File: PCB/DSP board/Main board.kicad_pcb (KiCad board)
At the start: 4 copper layers, 60 x 100 mm, 201 parts, among them J201 01x06 male SMD, J701 Conn_01x40_Female, J702 Conn_01x06_Female, J801 1140084168, J901 USB_B, U201 STM32H743II, U401 AS4C32M8SA, U501 CS42448, U601 MIC23050, U602 TPS2113A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

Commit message: Schematic updates + PCB placement
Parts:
- U604: footprint Housings_SSOP:TSOP-5_1.65x3.05mm_Pitch0.95mm -> TSOP-5:TSOP-5_1.65x3.05mm_Pitch0.95mm
- moved D101 252.8 mm to (254.5, 82.2)
- moved C614 238.9 mm to (253.6, 99.8), turned to 180 degrees
- moved C615 232.5 mm to (253.6, 101.0), turned to 180 degrees
- moved C504 231.7 mm to (248.2, 111.1), turned to 90 degrees
- moved C505 226.2 mm to (250.4, 115.3), turned to 270 degrees
- moved RN701 225.1 mm to (250.4, 32.6), turned to 270 degrees
- moved U604 224.8 mm to (253.5, 103.4), turned to 270 degrees
- moved C617 223.3 mm to (253.6, 105.8), turned to 180 degrees
- moved J801 222.1 mm to (226.4, 34.1)
- moved C503 219.0 mm to (231.6, 113.2), turned to 270 degrees
- moved RN702 215.0 mm to (251.7, 41.5), turned to 90 degrees
- moved RN703 213.4 mm to (246.6, 32.6), turned to 270 degrees
- moved C507 211.8 mm to (248.2, 113.9), turned to 270 degrees
- moved C506 209.2 mm to (240.9, 119.9), turned to 180 degrees
- moved RN705 202.0 mm to (242.4, 32.6), turned to 270 degrees
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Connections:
- RN502 pad 1: SAI2_SD_B -> Net-(RN502-Pad1)
- RN502 pad 2: SAI2_SCK_B -> SAI2_SD_B
- RN502 pad 3: SAI2_FS_B -> SAI2_SCK_B
- RN502 pad 4: Net-(RN502-Pad4) -> SAI2_FS_B
- RN502 pad 5: Net-(RN502-Pad5) -> DAC_LRCK
- RN502 pad 6: DAC_LRCK -> DAC_SCLK
- RN502 pad 7: DAC_SCLK -> DAC_SDIN1
- RN502 pad 8: DAC_SDIN1 -> Net-(RN502-Pad8)
- RN702 pad 1: Net-(RN702-Pad1) -> LCD_VSYNC
- RN702 pad 4: LCD_VSYNC -> Net-(RN702-Pad4)
- RN702 pad 5: TFT_VSD -> Net-(RN702-Pad5)
- RN702 pad 8: Net-(RN702-Pad8) -> TFT_VSD
- RN704 pad 1: LCD_B6 -> LCD_B0
- RN704 pad 2: LCD_B4 -> LCD_B2
- RN704 pad 3: LCD_B2 -> LCD_B4
- RN704 pad 4: LCD_B0 -> LCD_B6
- RN704 pad 5: TFT_B0 -> TFT_B6
- RN704 pad 6: TFT_B2 -> TFT_B4
- RN704 pad 7: TFT_B4 -> TFT_B2
- RN704 pad 8: TFT_B6 -> TFT_B0
- RN706 pad 1: LCD_G6 -> LCD_G0
- RN706 pad 2: LCD_G4 -> LCD_G2
- RN706 pad 3: LCD_G2 -> LCD_G4
- RN706 pad 4: LCD_G0 -> LCD_G6
- RN706 pad 5: TFT_G0 -> TFT_G6
- RN706 pad 6: TFT_G2 -> TFT_G4
- RN706 pad 7: TFT_G4 -> TFT_G2
- RN706 pad 8: TFT_G6 -> TFT_G0
- RN708 pad 1: LCD_R6 -> LCD_R0
- RN708 pad 2: LCD_R4 -> LCD_R2
- RN708 pad 3: LCD_R2 -> LCD_R4
- RN708 pad 4: LCD_R0 -> LCD_R6
- RN708 pad 5: TFT_R0 -> TFT_R6
- RN708 pad 6: TFT_R2 -> TFT_R4
- RN708 pad 7: TFT_R4 -> TFT_R2
- RN708 pad 8: TFT_R6 -> TFT_R0
- RN709 pad 1: TOUCH_NRESET -> TOUCH_NINT
- RN709 pad 2: TOUCH_NINT -> I2C1_SCL
- RN709 pad 3: I2C1_SCL -> I2C1_SDA
- RN709 pad 4: I2C1_SDA -> TOUCH_NRESET
- RN709 pad 5: TFT_SCL -> TFT_NRESET
- RN709 pad 7: TFT_NINT -> TFT_SCL
- RN709 pad 8: TFT_NRESET -> TFT_NINT
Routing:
- net GND: track 0.00 -> 855.7 mm, vias 0 -> 281
- added copper zone on B.Cu, net GND
- added copper zone on F.Cu, net GND

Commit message: Component Placement - RN
All components placed except for RAM Resistor Networks
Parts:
- removed C325: 1uF, Capacitors_SMD:C_0603
- removed C328: 10nF, Capacitors_SMD:C_0603
- moved R201 259.9 mm to (250.1, 66.8), turned to 90 degrees
- moved RN101 257.3 mm to (251.1, 83.7)
- moved RN102 251.8 mm to (253.2, 87.1), turned to 270 degrees
- moved R202 251.7 mm to (252.3, 79.5), turned to 270 degrees
- moved U603 243.1 mm to (238.6, 55.0), turned to 180 degrees
- moved D601 239.5 mm to (238.0, 52.9), turned to 180 degrees
- moved R606 235.1 mm to (235.1, 29.1), turned to 180 degrees
- moved C201 233.9 mm to (237.2, 61.5), turned to 270 degrees
- moved C701 233.3 mm to (236.2, 31.3)
- moved D602 231.4 mm to (234.6, 42.7), turned to 90 degrees
- moved C202 229.7 mm to (238.3, 61.5), turned to 270 degrees
- moved C702 228.5 mm to (236.5, 32.8)
- moved C205 227.4 mm to (251.3, 66.6), turned to 90 degrees
- moved C703 223.7 mm to (236.3, 34.2)
- moved L302 222.4 mm to (221.6, 59.7)
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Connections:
- D705 pad 1: TFT_NRESET -> TFT_SDA
- D705 pad 2: TFT_NINT -> TFT_NRESET
- D705 pad 4: TFT_SDA -> TFT_NINT
- D705 pad 7: TFT_SDA -> TFT_NINT
- D705 pad 8: TFT_NINT -> TFT_NRESET
- D705 pad 9: TFT_NRESET -> TFT_SDA
- RN709 pad 1: TOUCH_NINT -> I2C1_SDA
- RN709 pad 2: I2C1_SCL -> TOUCH_NRESET
- RN709 pad 3: I2C1_SDA -> TOUCH_NINT
- RN709 pad 4: TOUCH_NRESET -> I2C1_SCL
- RN709 pad 5: TFT_NRESET -> TFT_SCL
- RN709 pad 6: TFT_SDA -> TFT_NINT
- RN709 pad 7: TFT_SCL -> TFT_NRESET
- RN709 pad 8: TFT_NINT -> TFT_SDA
- RN801 pad 1: SDMMC1_D2 -> SDMMC1_CMD
- RN801 pad 4: SDMMC1_CMD -> SDMMC1_D2
- RN801 pad 5: SD_CMD -> SD_DAT2
- RN801 pad 8: SD_DAT2 -> SD_CMD
- RN802 pad 1: SDMMC1_CK -> SDMMC1_DETECT
- RN802 pad 2: SDMMC1_D0 -> SDMMC1_D1
- RN802 pad 3: SDMMC1_D1 -> SDMMC1_D0
- RN802 pad 4: SDMMC1_DETECT -> SDMMC1_CK
- RN802 pad 5: SD_DETECT -> SD_CLK
- RN802 pad 6: SD_DAT1 -> SD_DAT0
- RN802 pad 7: SD_DAT0 -> SD_DAT1
- RN802 pad 8: SD_CLK -> SD_DETECT
- U601 pad 6: (no net) -> GND

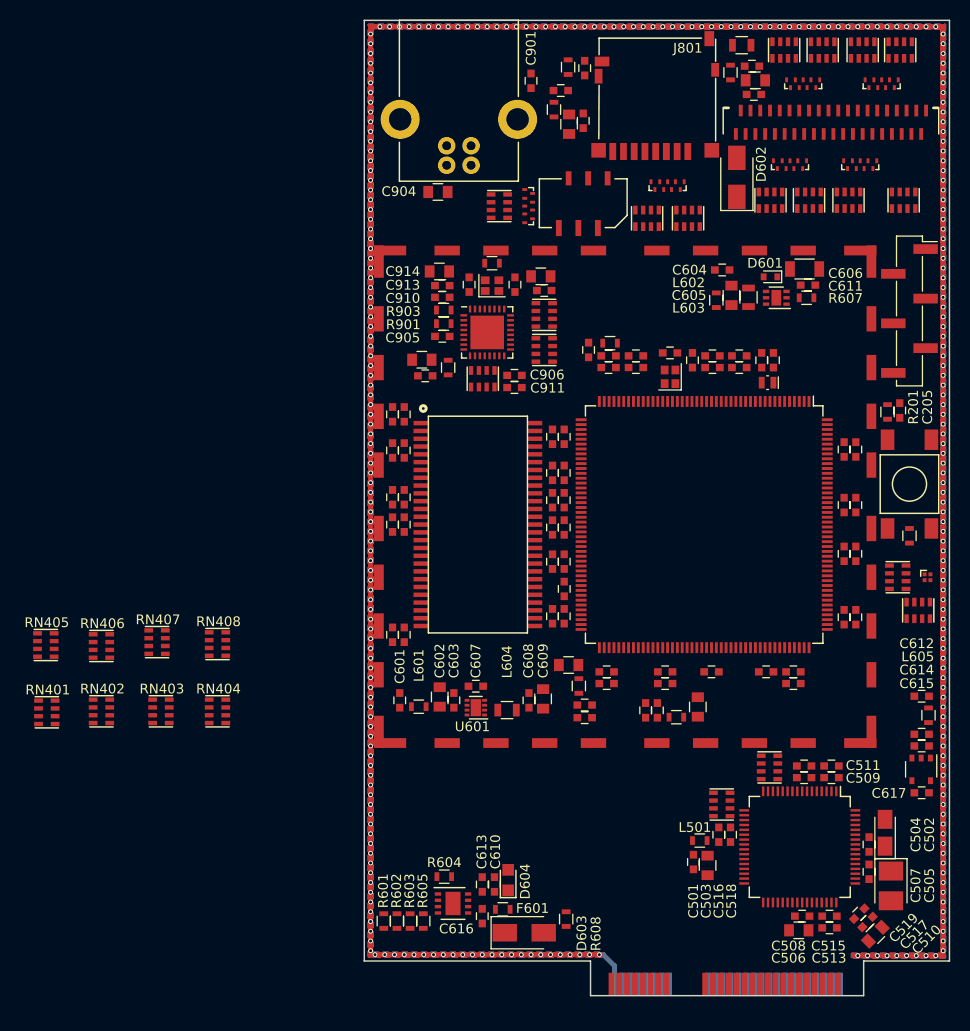
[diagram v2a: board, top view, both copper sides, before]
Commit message: RAM Routing - Data
All RAM routing & matching done, supply still needs to be done
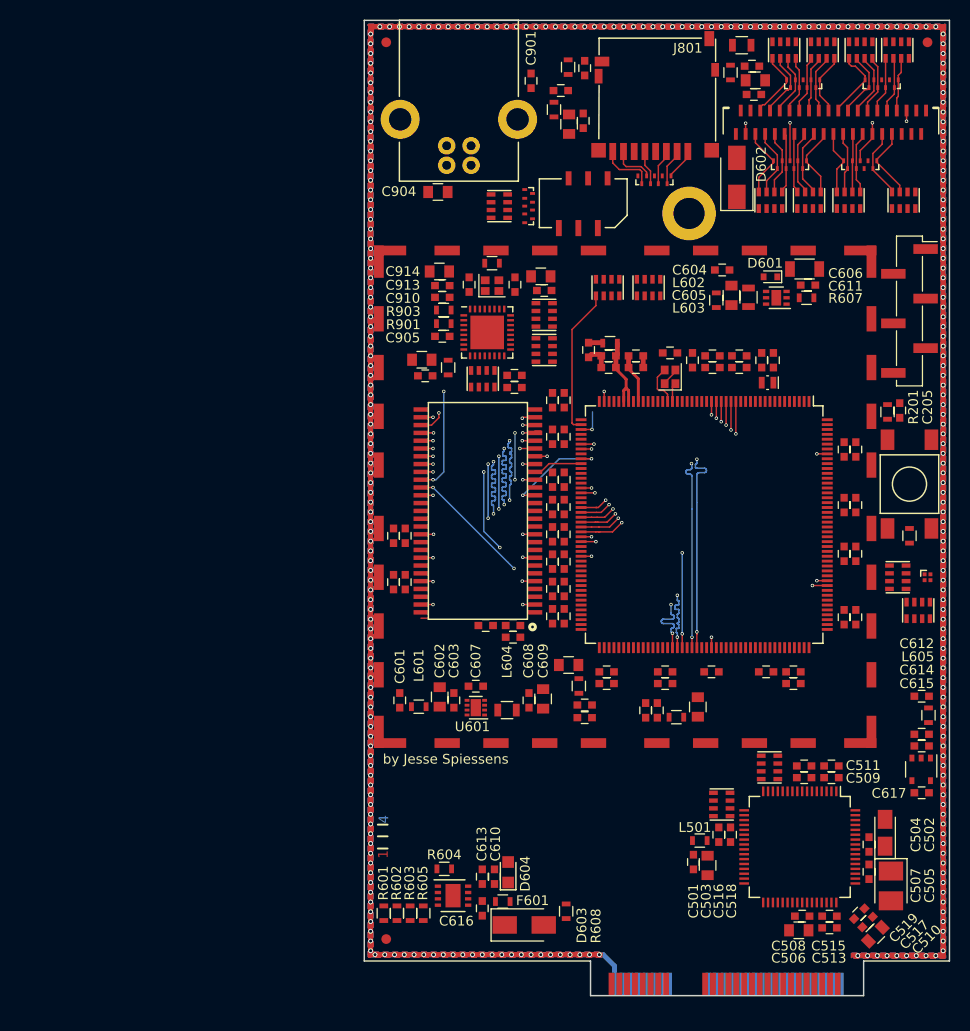
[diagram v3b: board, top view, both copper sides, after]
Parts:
- removed RN401, RN402, RN403, RN404, RN405, RN406, RN407, RN408: 51R, Resistor:0603_RN4
- added REF**: Fiducial_1mm_Dia_2.54mm_Outer_CopperTop, Fiducials:Fiducial_1mm_Dia_2.54mm_Outer_CopperTop, F.Cu at (198.7, 28.9)
- added REF**: Fiducial_1mm_Dia_2.54mm_Outer_CopperTop, Fiducials:Fiducial_1mm_Dia_2.54mm_Outer_CopperTop, F.Cu at (198.7, 120.8)
- added REF**: Fiducial_1mm_Dia_2.54mm_Outer_CopperTop, Fiducials:Fiducial_1mm_Dia_2.54mm_Outer_CopperTop, F.Cu at (254.2, 28.9)
- added REF**: MountingHole_3.2mm_M3_ISO14580_Pad, Mounting_Holes:MountingHole_3.2mm_M3_ISO14580_Pad, F.Cu at (229.7, 46.4)
- moved C412 29.8 mm to (216.9, 65.5), turned to 90 degrees
- moved C413 28.5 mm to (215.7, 65.5), turned to 90 degrees
- moved C404 26.0 mm to (211.7, 89.8), turned to 180 degrees
- moved C405 24.4 mm to (211.7, 88.7), turned to 180 degrees
- moved C406 19.6 mm to (216.9, 79.3), turned to 90 degrees
- moved C416 18.7 mm to (199.4, 79.5)
- moved C414 18.4 mm to (199.4, 84.2)
- moved C409 17.9 mm to (215.7, 84.9), turned to 90 degrees
- moved C410 17.7 mm to (216.9, 76.5), turned to 270 degrees
- moved C407 17.5 mm to (215.7, 79.3), turned to 90 degrees
- moved C417 16.4 mm to (200.6, 79.5)
- moved C408 16.3 mm to (208.8, 88.7), turned to 0 degrees
- moved C415 16.1 mm to (200.6, 84.2)
- moved C411 15.3 mm to (215.7, 76.5), turned to 270 degrees
- moved RN802 8.17 mm to (221.3, 54.0)
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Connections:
- D701 pad 2: TFT_CLKIN -> Net-(D701-Pad2)
- D701 pad 8: Net-(D701-Pad8) -> TFT_CLKIN
- D702 pad 9: Net-(D702-Pad9) -> TFT_STBYB
- EMI101 pad 2: Net-(EMI101-Pad2) -> GND
- EMI101 pad 3: Net-(EMI101-Pad3) -> GND
- EMI101 pad 4: Net-(EMI101-Pad4) -> GND
- EMI101 pad 5: Net-(EMI101-Pad5) -> GND
- EMI101 pad 6: Net-(EMI101-Pad6) -> GND
- EMI101 pad 7: Net-(EMI101-Pad7) -> GND
- EMI101 pad 8: Net-(EMI101-Pad8) -> GND
- EMI101 pad 9: Net-(EMI101-Pad9) -> GND
- RN702 pad 1: LCD_VSYNC -> LCD_STBYB
- RN702 pad 2: Net-(RN702-Pad2) -> LCD_VSYNC
- RN702 pad 7: Net-(RN702-Pad7) -> TFT_VSD
- RN702 pad 8: TFT_VSD -> TFT_STBYB
- U201 pad 8: TFT_STBYB -> LCD_STBYB
- U401 pad 11: RAM_DQ3 -> FMC_D3
- U401 pad 16: RAM_WE# -> FMC_SDNWE
- U401 pad 17: RAM_CAS# -> FMC_SDNCAS
- U401 pad 18: RAM_RAS# -> FMC_SDNRAS
- U401 pad 19: RAM_CS# -> FMC_SDNE0
- U401 pad 2: RAM_DQ0 -> FMC_D0
- U401 pad 20: RAM_BA0 -> FMC_BA0
- U401 pad 21: RAM_BA1 -> FMC_BA1
- U401 pad 22: RAM_A10 -> FMC_A10
- U401 pad 23: RAM_A0 -> FMC_A0
- U401 pad 24: RAM_A1 -> FMC_A1
- U401 pad 25: RAM_A2 -> FMC_A2
- U401 pad 26: RAM_A3 -> FMC_A3
- U401 pad 29: RAM_A4 -> FMC_A4
- U401 pad 30: RAM_A5 -> FMC_A5
- U401 pad 31: RAM_A6 -> FMC_A6
- U401 pad 32: RAM_A7 -> FMC_A7
- U401 pad 33: RAM_A8 -> FMC_A8
- U401 pad 34: RAM_A9 -> FMC_A9
- U401 pad 35: RAM_A11 -> FMC_A11
- U401 pad 36: RAM_A12 -> FMC_A12
- U401 pad 37: RAM_CKE -> FMC_SDCKE0
- U401 pad 38: RAM_CLK -> FMC_SDCLK
- U401 pad 39: RAM_DQM -> FMC_NBL0
- U401 pad 44: RAM_DQ4 -> FMC_D4
- U401 pad 47: RAM_DQ5 -> FMC_D5
- U401 pad 5: RAM_DQ1 -> FMC_D1
- U401 pad 50: RAM_DQ6 -> FMC_D6
- U401 pad 53: RAM_DQ7 -> FMC_D7
- U401 pad 8: RAM_DQ2 -> FMC_D2
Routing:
- net FMC_NBL0: track 0.00 -> 43.9 mm, vias 0 -> 2
- net FMC_A12: track 0.00 -> 43.6 mm, vias 0 -> 5
- net FMC_D4: track 0.00 -> 40.2 mm, vias 0 -> 2
- net FMC_A1: track 0.00 -> 39.0 mm, vias 0 -> 2
- net FMC_A7: track 0.00 -> 38.7 mm, vias 0 -> 4
- net FMC_A6: track 0.00 -> 38.4 mm, vias 0 -> 4
- net FMC_D2: track 0.00 -> 38.4 mm, vias 0 -> 2
- net FMC_D7: track 0.00 -> 38.4 mm, vias 0 -> 2
- net FMC_A0: track 0.00 -> 38.3 mm, vias 0 -> 2
- net FMC_BA1: track 0.00 -> 38.3 mm, vias 0 -> 3
- net FMC_SDCLK: track 0.00 -> 38.3 mm, vias 0 -> 3
- net FMC_A4: track 0.00 -> 38.3 mm, vias 0 -> 2
- net FMC_D3: track 0.00 -> 38.3 mm, vias 0 -> 2
- net FMC_BA0: track 0.00 -> 38.3 mm, vias 0 -> 3
- net FMC_A5: track 0.00 -> 38.2 mm, vias 0 -> 2
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- added copper zone on In1.Cu, net GND
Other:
- rule trace_min: 0.1524 -> 0.15
- board text added: "1"
- board text added: "2"
- board text added: "3"
- board text added: "4"
- board text added: "by Jesse Spiessens"

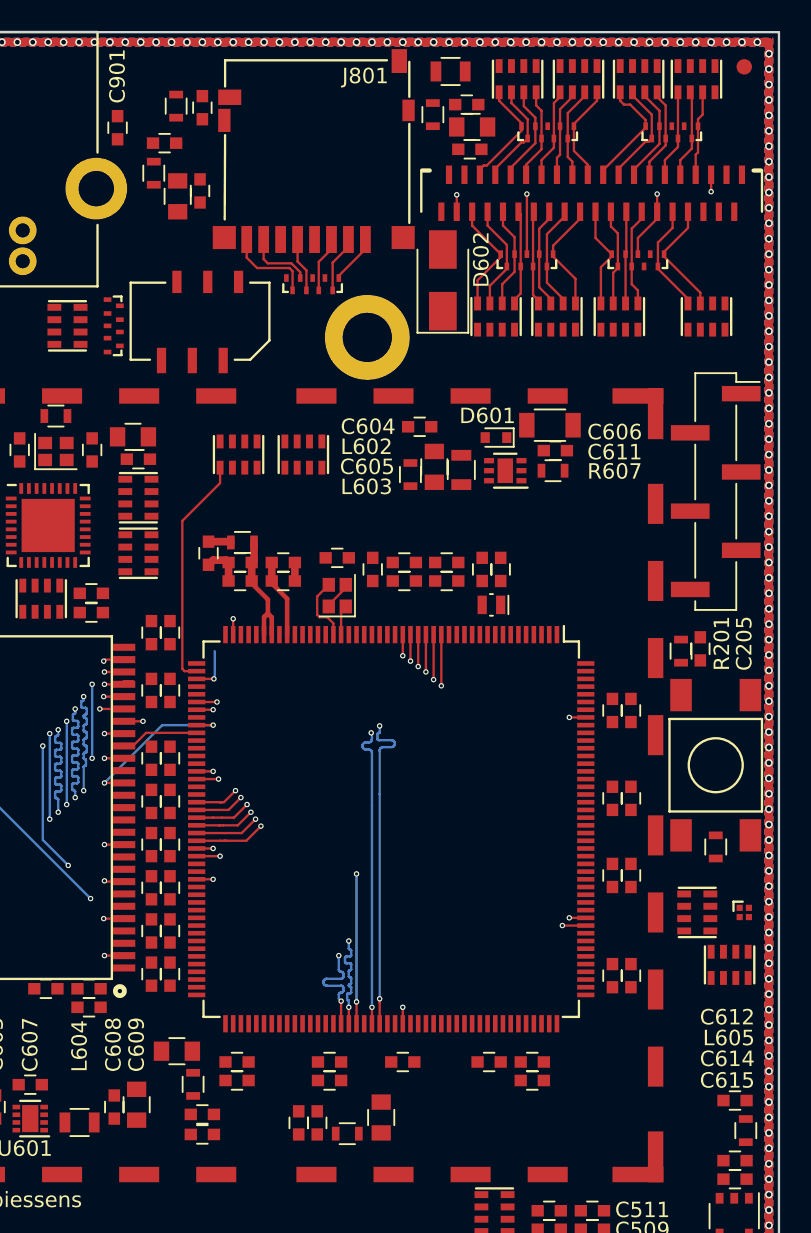
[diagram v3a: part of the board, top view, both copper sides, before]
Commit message: RAM + Display
Ram & display routed + matched-ish
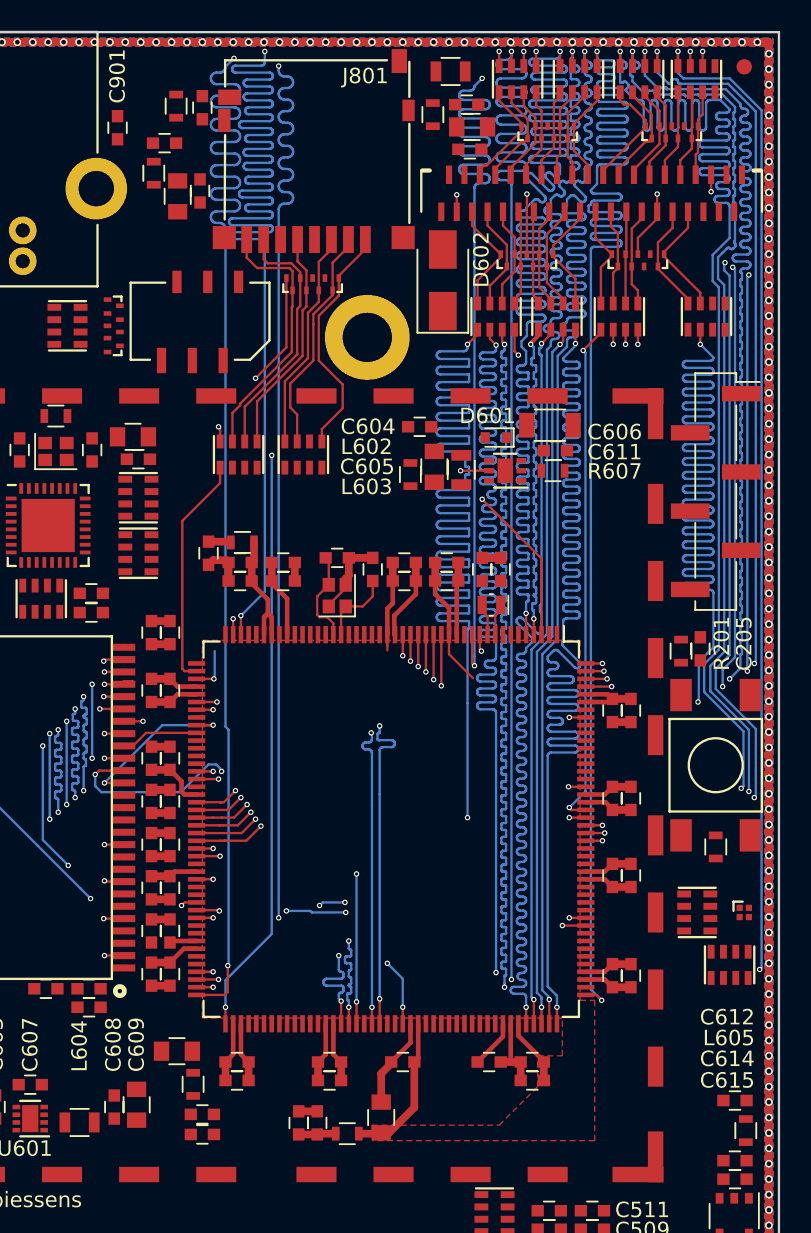
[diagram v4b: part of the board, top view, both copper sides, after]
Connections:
- U201 pad 7: BAT_POWER -> Net-(U201-Pad7)
- U201 pad 84: Net-(U201-Pad84) -> BAT_POWER
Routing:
- net LCD_G1: track 0.00 -> 126.5 mm, vias 0 -> 2
- net LCD_R6: track 0.00 -> 103.5 mm, vias 0 -> 3
- net LCD_CLK: track 0.00 -> 103.3 mm, vias 0 -> 5
- net LCD_B1: track 0.00 -> 103.2 mm, vias 0 -> 3
- net LCD_R0: track 0.00 -> 103.2 mm, vias 0 -> 3
- net LCD_G7: track 0.00 -> 103.2 mm, vias 0 -> 2
- net LCD_B2: track 0.00 -> 103.2 mm, vias 0 -> 4
- net LCD_G6: track 0.00 -> 103.2 mm, vias 0 -> 2
- net LCD_R2: track 0.00 -> 103.2 mm, vias 0 -> 3
- net LCD_HSYNC: track 0.00 -> 103.2 mm, vias 0 -> 3
- net LCD_VSYNC: track 0.00 -> 103.2 mm, vias 0 -> 3
- net LCD_R1: track 0.00 -> 103.2 mm, vias 0 -> 3
- net LCD_R7: track 0.00 -> 103.2 mm, vias 0 -> 4
- net LCD_R3: track 0.00 -> 103.2 mm, vias 0 -> 3
- net LCD_R5: track 0.00 -> 103.2 mm, vias 0 -> 3
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- added copper zone on F.Cu, net +3V3_MCU
